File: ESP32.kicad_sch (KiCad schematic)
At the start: 30 parts, among them J201 GPIO, J202 Power, J203 Conn_01x01, J206 IO, J207 Conn_01x07, U201 ESP32-WROOM-32E

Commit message: HALMET redesign
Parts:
- removed J202: Power, Connector_PinHeader_2.54mm:PinHeader_2x03_P2.54mm_Vertical, symbol Connector_Generic:Conn_02x03_Odd_Even
- removed J206: IO, SH-ESP32:PinHeader_1x07_P2.54mm_Vertical-RoundP1, symbol Connector_Generic:Conn_01x07
- removed J207: Conn_01x07, SH-ESP32:PinHeader_1x07_P2.54mm_Vertical-RoundP1, symbol Connector_Generic:Conn_01x07
- removed JP201, JP202, JP203, JP204, JP205, JP206, JP207, JP208, JP209: SolderJumper_2_Open, SH-ESP32:SolderJumper-2_P1.3mm_Open_TrianglePad_Narrow, symbol Jumper:SolderJumper_2_Open
- removed R202, R203, R204, R205, R206, R207, R208, R209, R210: 0R, Resistor_SMD:R_0603_1608Metric, symbol Device:R
- added J302: Conn_01x02, Connector_PinHeader_2.54mm:PinHeader_1x02_P2.54mm_Vertical, symbol Connector_Generic:Conn_01x02
- J201: footprint Connector_PinHeader_2.54mm:PinHeader_2x20_P2.54mm_Vertical -> Connector_PinHeader_2.54mm:PinHeader_2x10_P2.54mm_Vertical; symbol Connector_Generic:Conn_02x20_Odd_Even -> Connector_Generic:Conn_02x10_Odd_Even; LCSC C429965 -> (none)
- J203: footprint Connector_PinHeader_2.54mm:PinHeader_1x01_P2.54mm_Vertical -> TestPoint:TestPoint_Pad_D2.0mm; now left out of the parts list
- U201: value ESP32-WROOM-32E -> ESP32-WROOM-32; footprint SH-ESP32:ESP32-WROOM-32-HandSolder -> RF_Module:ESP32-WROOM-32; symbol RF_Module:ESP32-WROOM-32D -> RF_Module:ESP32-WROOM-32; JLCPCB_CORRECTION 0;0.8;270 -> (none)
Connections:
- net IO4 is gone; now on net DQ: U201.26 (IO4)
- net RXD0 is gone; now on net USB_TXD: U201.34 (RXD0/IO3)
- net RXD0_C is gone; now on net GND: J201.18 (Pin_18)
- net TXD0 is gone; now on net USB_RXD: U201.35 (TXD0/IO1)
- net TXD0_C is gone; now on net GND: J201.16 (Pin_16)
- net CAN_RX: now also U201.30 (IO18)
- net CAN_TX: now also U201.31 (IO19)
- net EN: now also J302.1 (Pin_1); no longer J201.24 (Pin_24)
- net GND: now also J201.12 (Pin_12), J201.2 (Pin_2); no longer J201.10 (Pin_10), J201.11 (Pin_11), J201.20 (Pin_20), J201.29 (Pin_29), J201.37 (Pin_37), J201.38 (Pin_38), J201.39 (Pin_39), J201.40 (Pin_40)
- net IO0: now also J302.2 (Pin_2); no longer J201.12 (Pin_12)
- net IO16: now also J201.7 (Pin_7)
- net IO17: now also J201.5 (Pin_5)
- net IO32: now also J201.8 (Pin_8)
- net IO33: now also J201.9 (Pin_9)
- net IO34: now also J201.10 (Pin_10)
- net IO35: now also J201.11 (Pin_11)
- net IO5: now also J201.3 (Pin_3); no longer J201.6 (Pin_6)
- net SCL: now also U201.36 (IO22)
- net SDA: now also U201.33 (IO21)
- net SENSOR_VN: now also J201.6 (Pin_6); no longer J201.17 (Pin_17)
- net SENSOR_VP: now also J201.4 (Pin_4); no longer J201.15 (Pin_15)
- net +3V3 renamed +3.3V
- net +3.3V: now also J201.1 (Pin_1), J201.20 (Pin_20); no longer J201.13 (Pin_13), J201.19 (Pin_19), J201.35 (Pin_35), J201.36 (Pin_36)
- net IO12 renamed TDI
- net TDI: now also J201.13 (Pin_13); no longer J201.21 (Pin_21)
- net IO13 renamed TCK
- net TCK: now also J201.17 (Pin_17); no longer J201.25 (Pin_25)
- net IO14 renamed TMS
- net TMS: now also J201.19 (Pin_19); no longer J201.23 (Pin_23)
- net IO15 renamed TDO
- net TDO: now also J201.15 (Pin_15); no longer J201.27 (Pin_27)
- removed net IO16_C_SDA: J201.32 (Pin_32)
- removed net IO17_C_SCL: J201.34 (Pin_34)
- removed net IO18: J201.5 (Pin_5), U201.30 (IO18)
- removed net IO19: J201.4 (Pin_4), U201.31 (IO19)
- removed net IO21: J201.3 (Pin_3), U201.33 (IO21)
- removed net IO22: J201.2 (Pin_2), U201.36 (IO22)
- net IO23 renamed DI1
- net DI1: no longer J201.1 (Pin_1)
- net IO25 renamed DI2
- net DI2: no longer J201.8 (Pin_8)
- net IO26 renamed DI3
- net DI3: no longer J201.7 (Pin_7)
- net IO27 renamed DI4
- net DI4: no longer J201.9 (Pin_9)
- removed net IO32_C: J201.28 (Pin_28)
- removed net IO33_C: J201.26 (Pin_26)
- removed net IO34_C: J201.31 (Pin_31)
- removed net IO35_C: J201.30 (Pin_30)
- removed net IO4_C: J201.33 (Pin_33)
- net LED renamed IO2
- net IO2: no longer J201.22 (Pin_22)
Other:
- note removed: "0R jumpers allow for rerouting and disabling peripherals"
- note removed: "NOTE: TX/RX Crossover RXD0 -> USB_TXD TXD0 -> USB_RXD"
- note removed: "PHY_MDC"
- note removed: "PHY_MDIO"
- note removed: "PHY_RESET_N"
- note removed: "RMII Ethernet"
- note removed: "RMII_EN"
- note removed: "RMII_RXD0"
- note removed: "RMII_RXD1"
- note removed: "RMII_TXD0"
- note removed: "RMII_TXD1"
- note removed: "RMI_CRS_DV"
- note removed: "Solder jumpers allow for rerouting peripherals GPIOs to J201"
- note removed: "UART0"
- title: Sailor Hat with ESP32 -> Hat Labs Marine Engine/Tank interface (HALMET)
- moved on the sheet: J203

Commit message: Substitute parts according to availability
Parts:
- C203: value 1uf -> 1uF
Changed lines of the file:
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@@
       (effects (font (size 1.27 1.27)) (justify left))
     )
-    (property "Value" "1uf" (at 66.421 176.403 0)
+    (property "Value" "1uF" (at 66.421 176.403 0)
       (effects (font (size 1.27 1.27)) (justify left))
     )

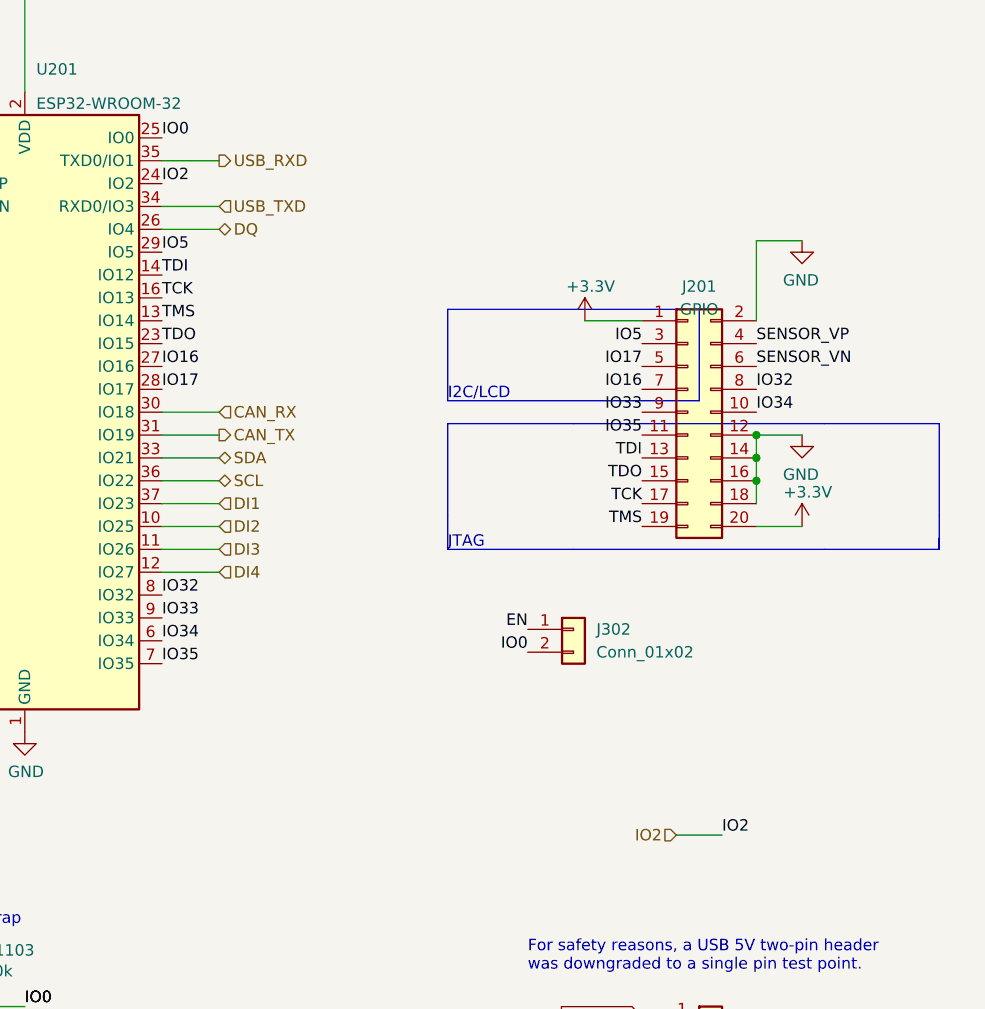
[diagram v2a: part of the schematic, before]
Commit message: Implement HALMET v1.0.0 design changes
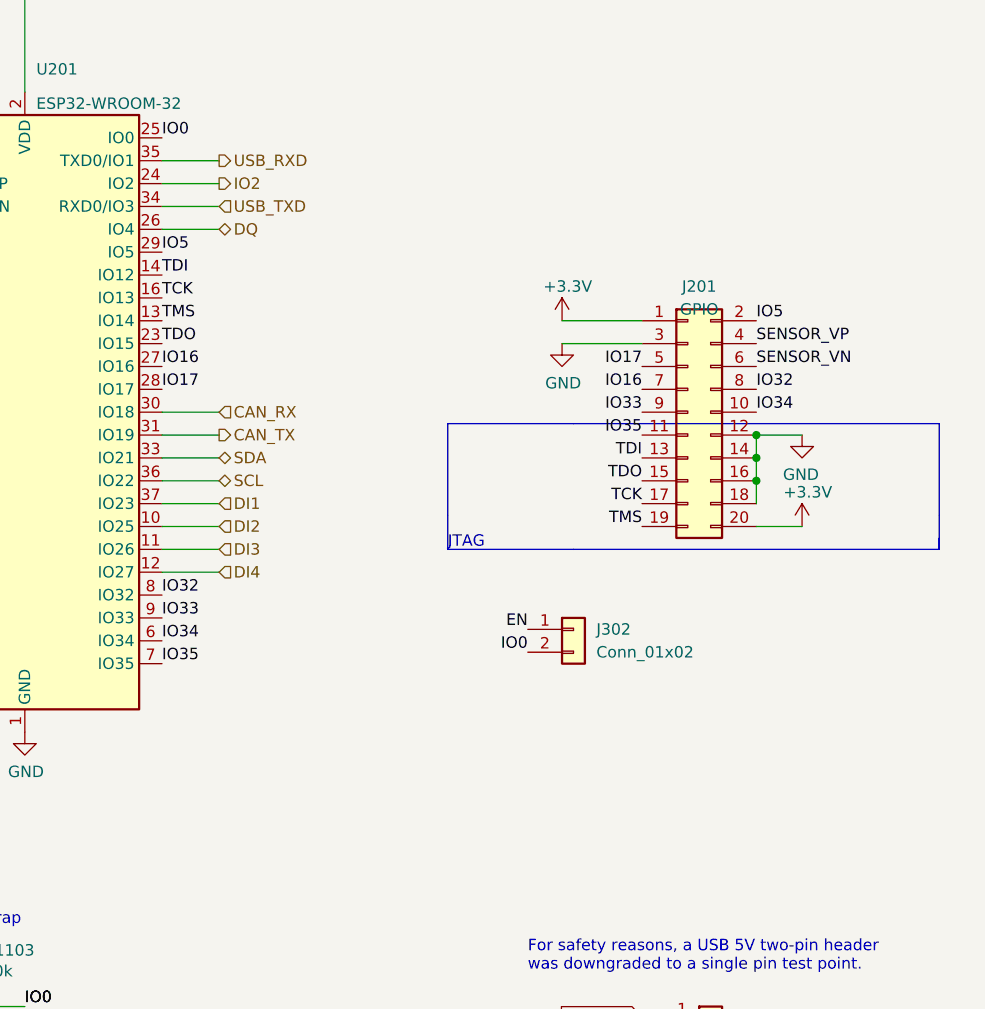
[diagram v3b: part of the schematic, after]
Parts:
- U201: JLCPCB_CORRECTION (none) -> 0;0;270
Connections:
- net GND: now also J201.3 (Pin_3); no longer J201.2 (Pin_2)
- net IO5: now also J201.2 (Pin_2); no longer J201.3 (Pin_3)
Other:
- note removed: "I2C/LCD"
- title: Hat Labs Marine Engine/Tank interface (HALMET) -> Hat Labs Marine Engine & Tank interface (HALMET)
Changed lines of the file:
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@@
   (paper "A4")
   (title_block
-    (title "Hat Labs Marine Engine/Tank interface (HALMET)")
-    (date "2023-09-19")
-    (rev "1.0.0-a1")
+    (title "Hat Labs Marine Engine & Tank interface (HALMET)")
+    (date "2023-11-27")
+    (rev "1.0.0")
     (company "Hat Labs Ltd")
     (comment 1 "https://creativecommons.org/licenses/by-sa/4.0")
@@
     (stroke (width 0) (type default))
   )
-  (polyline (pts (xy 111.76 62.23) (xy 139.7 62.23))
-    (stroke (width 0) (type default))
-  )
   (polyline (pts (xy 111.76 88.9) (xy 125.73 88.9))
     (stroke (width 0) (type default))
   )
-  (polyline (pts (xy 139.7 72.39) (xy 111.76 72.39))
-    (stroke (width 0) (type default))
-  )
   (wire (pts (xy 64.77 25.4) (xy 55.88 25.4))
     (stroke (width 0) (type default))
@@
     (stroke (width 0) (type default))
   )
-  (polyline (pts (xy 139.7 72.39) (xy 139.7 62.23))
-    (stroke (width 0) (type default))
-  )
   (wire (pts (xy 146.05 81.28) (xy 146.05 83.82))
     (stroke (width 0) (type default))
@@
     (stroke (width 0) (type default))
   )
-  (wire (pts (xy 146.05 54.61) (xy 146.05 63.5))
-    (stroke (width 0) (type default))
-  )
   (wire (pts (xy 86.36 53.34) (xy 80.01 53.34))
     (stroke (width 0) (type default))
@@
     (stroke (width 0) (type default))
   )
-  (wire (pts (xy 133.35 63.5) (xy 127 63.5))
+  (wire (pts (xy 133.35 63.5) (xy 124.46 63.5))
     (stroke (width 0) (type default))
   )
@@
     (stroke (width 0) (type default))
   )
-  (polyline (pts (xy 111.76 72.39) (xy 111.76 62.23))
-    (stroke (width 0) (type default))
-  )
   (wire (pts (xy 64.77 25.4) (xy 64.77 38.1))
     (stroke (width 0) (type default))
@@
     (stroke (width 0) (type default))
   )
-  (wire (pts (xy 137.16 120.65) (xy 142.24 120.65))
-    (stroke (width 0) (type default))
-  )
-  (wire (pts (xy 151.13 54.61) (xy 146.05 54.61))
+  (wire (pts (xy 124.46 66.04) (xy 133.35 66.04))
+    (stroke (width 0) (type default))
+  )
+  (wire (pts (xy 80.01 48.26) (xy 86.36 48.26))
     (stroke (width 0) (type default))
   )
@@
   )
   (text "Strap" (at 59.69 130.81 0)
-    (effects (font (size 1.27 1.27)) (justify left bottom))
-  )
-  (text "I2C/LCD" (at 111.76 72.39 0)
     (effects (font (size 1.27 1.27)) (justify left bottom))
   )
@@
     (effects (font (size 1.27 1.27)) (justify left bottom))
   )
-  (label "IO5" (at 133.35 66.04 180) (fields_autoplaced)
-    (effects (font (size 1.27 1.27)) (justify right bottom))
+  (label "IO5" (at 146.05 63.5 0) (fields_autoplaced)
+    (effects (font (size 1.27 1.27)) (justify left bottom))
   )
   (label "IO16" (at 80.01 68.58 0) (fields_autoplaced)
@@
     (effects (font (size 1.27 1.27)) (justify left bottom))
   )
-  (label "IO2" (at 80.01 48.26 0) (fields_autoplaced)
-    (effects (font (size 1.27 1.27)) (justify left bottom))
-  )
   (label "IO35" (at 133.35 76.2 180) (fields_autoplaced)
     (effects (font (size 1.27 1.27)) (justify right bottom))
@@
   )
   (label "IO0" (at 80.01 43.18 0) (fields_autoplaced)
-    (effects (font (size 1.27 1.27)) (justify left bottom))
-  )
-  (label "IO2" (at 142.24 120.65 0) (fields_autoplaced)
     (effects (font (size 1.27 1.27)) (justify left bottom))
   )
@@
     (effects (font (size 1.27 1.27)) (justify right))
   )
-  (hierarchical_label "IO2" (shape input) (at 137.16 120.65 180) (fields_autoplaced)
-    (effects (font (size 1.27 1.27)) (justify right))
+  (hierarchical_label "IO2" (shape output) (at 86.36 48.26 0) (fields_autoplaced)
+    (effects (font (size 1.27 1.27)) (justify left))
   )
   (hierarchical_label "DQ" (shape bidirectional) (at 86.36 53.34 0) (fields_autoplaced)
@@
     )
     (property "LCSC" "C701341" (at 64.77 73.66 0)
+      (effects (font (size 1.27 1.27)) hide)
+    )
+    (property "JLCPCB_CORRECTION" "0;0;270" (at 64.77 73.66 0)
       (effects (font (size 1.27 1.27)) hide)
     )
@@
     )
   )
-  (symbol (lib_id "power:+3.3V") (at 127 63.5 0) (unit 1)
-    (in_bom yes) (on_board yes) (dnp no)
-    (property "Reference" "#PWR0113" (at 127 67.31 0)
-      (effects (font (size 1.27 1.27)) hide)
-    )
-    (property "Value" "+3.3V" (at 127.635 59.69 0)
-      (effects (font (size 1.27 1.27)))
-    )
-    (property "Footprint" "" (at 127 63.5 0)
-      (effects (font (size 1.27 1.27)) hide)
-    )
-    (property "Datasheet" "" (at 127 63.5 0)
+  (symbol (lib_id "power:+3.3V") (at 124.46 63.5 0) (unit 1)
+    (in_bom yes) (on_board yes) (dnp no)
+    (property "Reference" "#PWR0113" (at 124.46 67.31 0)
+      (effects (font (size 1.27 1.27)) hide)
+    )
+    (property "Value" "+3.3V" (at 125.095 59.69 0)
+      (effects (font (size 1.27 1.27)))
+    )
+    (property "Footprint" "" (at 124.46 63.5 0)
+      (effects (font (size 1.27 1.27)) hide)
+    )
+    (property "Datasheet" "" (at 124.46 63.5 0)
       (effects (font (size 1.27 1.27)) hide)
     )
@@
     )
   )
-  (symbol (lib_id "power:GND") (at 151.13 54.61 0) (mirror y) (unit 1)
-    (in_bom yes) (on_board yes) (dnp no)
-    (property "Reference" "#PWR0114" (at 151.13 60.96 0)
-      (effects (font (size 1.27 1.27)) hide)
-    )
-    (property "Value" "GND" (at 151.003 59.0042 0)
-      (effects (font (size 1.27 1.27)))
-    )
-    (property "Footprint" "" (at 151.13 54.61 0)
-      (effects (font (size 1.27 1.27)) hide)
-    )
-    (property "Datasheet" "" (at 151.13 54.61 0)
-      (effects (font (size 1.27 1.27)) hide)
-    )
+  (symbol (lib_id "power:GND") (at 124.46 66.04 0) (unit 1)
+    (in_bom yes) (on_board yes) (dnp no)
+    (property "Reference" "#PWR0114" (at 124.46 72.39 0)
+      (effects (font (size 1.27 1.27)) hide)
+    )
+    (property "Value" "GND" (at 124.587 70.4342 0)
+      (effects (font (size 1.27 1.27)))
+    )
+    (property "Footprint" "" (at 124.46 66.04 0)
+      (effects (font (size 1.27 1.27)) hide)
+    )
+    (property "Datasheet" "" (at 124.46 66.04 0)
+      (effects (font (size 1.27 1.27)) hide)
+    )

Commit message: Update parts according to availability
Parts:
- C202: value 22uF/6.3V -> 22uF
- U201: value ESP32-WROOM-32 -> ESP32-WROOM-32E-N16; LCSC C701341 -> C701343
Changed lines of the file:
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@@
       (effects (font (size 1.27 1.27)) (justify left))
     )
-    (property "Value" "ESP32-WROOM-32" (at 66.04 39.37 0)
+    (property "Value" "ESP32-WROOM-32E-N16" (at 66.04 39.37 0)
       (effects (font (size 1.27 1.27)) (justify left))
     )
@@
       (effects (font (size 1.27 1.27)) hide)
     )
-    (property "LCSC" "C701341" (at 64.77 73.66 0)
+    (property "LCSC" "C701343" (at 64.77 73.66 0)
       (effects (font (size 1.27 1.27)) hide)
     )
@@
       (effects (font (size 1.27 1.27)) (justify left))
     )
-    (property "Value" "22uF/6.3V" (at 52.959 29.337 0)
+    (property "Value" "22uF" (at 52.959 29.337 0)
       (effects (font (size 1.27 1.27)) (justify left))
     )

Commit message: Fix DI4 & DI3 pins
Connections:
- net DI3: now also U201.12 (IO27); no longer U201.11 (IO26)
- net DI4: now also U201.11 (IO26); no longer U201.12 (IO27)
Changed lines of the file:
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@@
     )
   )
-  (hierarchical_label "DI3" (shape input) (at 86.36 88.9 0) (fields_autoplaced)
+  (hierarchical_label "DI3" (shape input) (at 86.36 91.44 0) (fields_autoplaced)
     (effects (font (size 1.27 1.27)) (justify left))
   )
@@
     (effects (font (size 1.27 1.27)) (justify left))
   )
-  (hierarchical_label "DI4" (shape input) (at 86.36 91.44 0) (fields_autoplaced)
+  (hierarchical_label "DI4" (shape input) (at 86.36 88.9 0) (fields_autoplaced)
     (effects (font (size 1.27 1.27)) (justify left))
   )

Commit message: Update parts according to availability
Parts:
- D1101, D1102: LCSC C134404 -> C78261
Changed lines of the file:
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@@
       (effects (font (size 1.27 1.27)) hide)
     )
-    (property "LCSC" "C134404" (at 46.99 139.7 90)
+    (property "LCSC" "C78261" (at 46.99 139.7 90)
       (effects (font (size 1.27 1.27)) hide)
     )
@@
       (effects (font (size 1.27 1.27)) hide)
     )
-    (property "LCSC" "C134404" (at 46.99 171.45 90)
+    (property "LCSC" "C78261" (at 46.99 171.45 90)
       (effects (font (size 1.27 1.27)) hide)
     )

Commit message: Save with a newer KiCad; change parts for availability; fix rotations
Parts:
- U201: JLCPCB_CORRECTION 0;0;270 -> 0;0.75;270
